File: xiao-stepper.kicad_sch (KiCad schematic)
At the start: 16 parts, among them J1 Conn_PinHeader_1x04_P2.54mm_H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, M1 XIAO-RP2040_SocketSMD

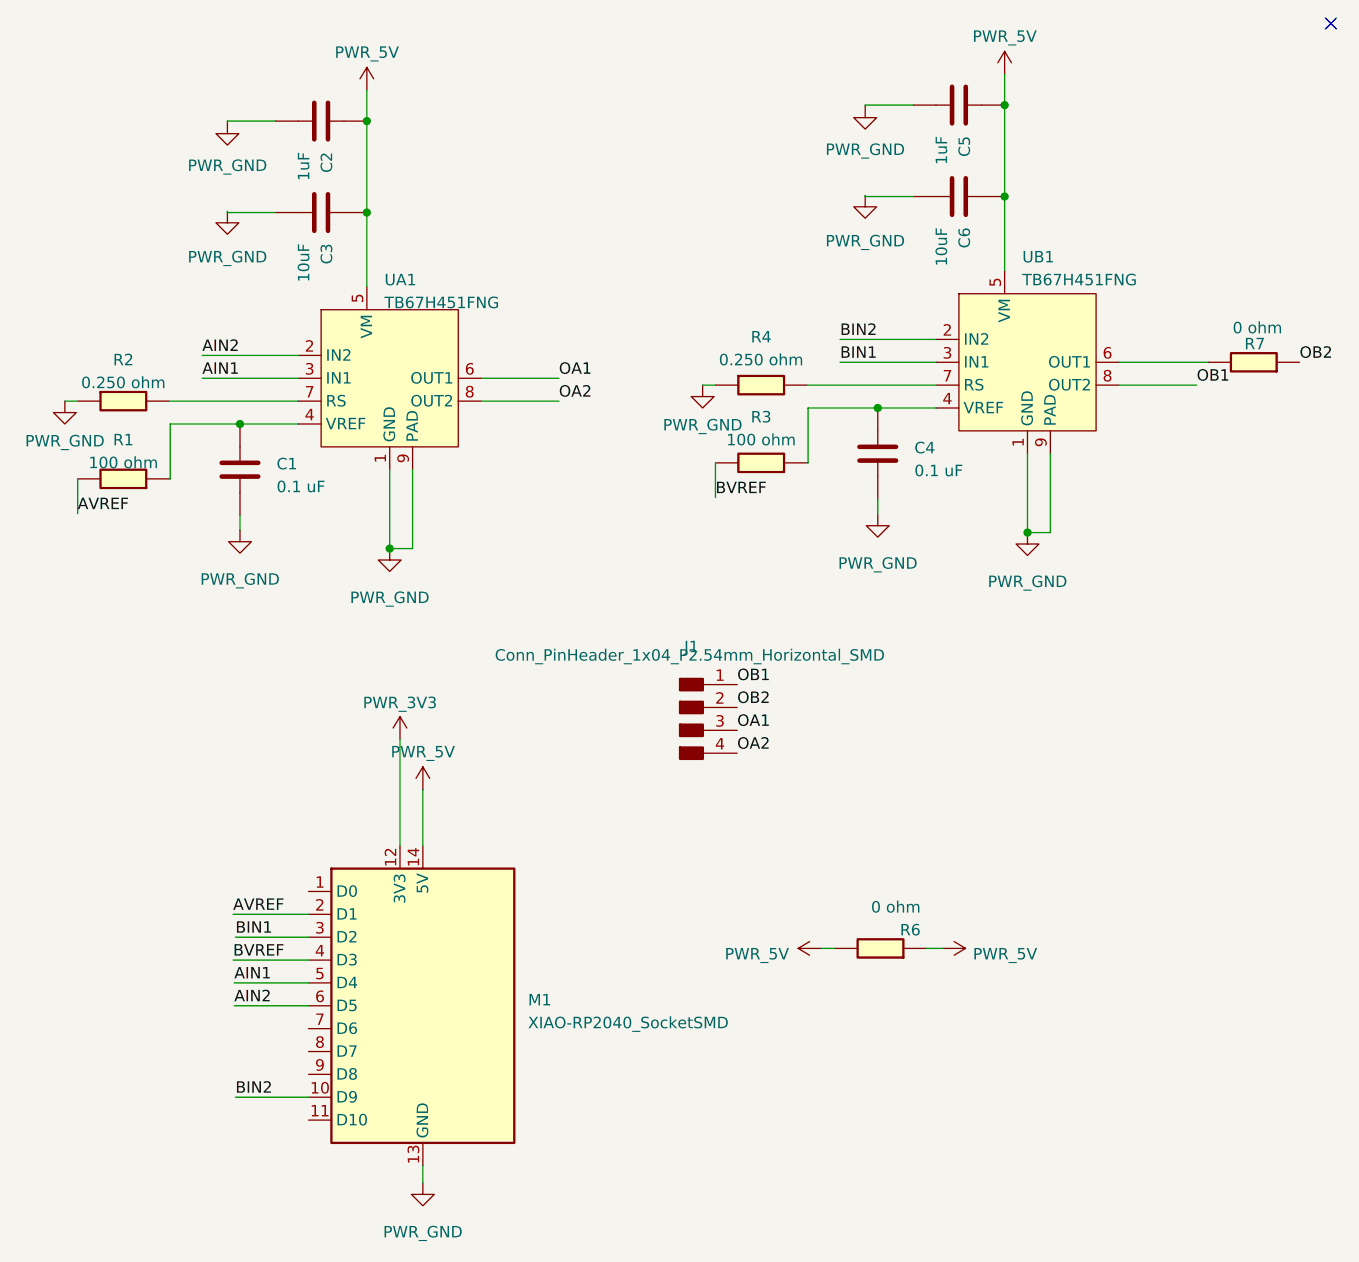
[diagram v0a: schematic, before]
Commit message: Added images
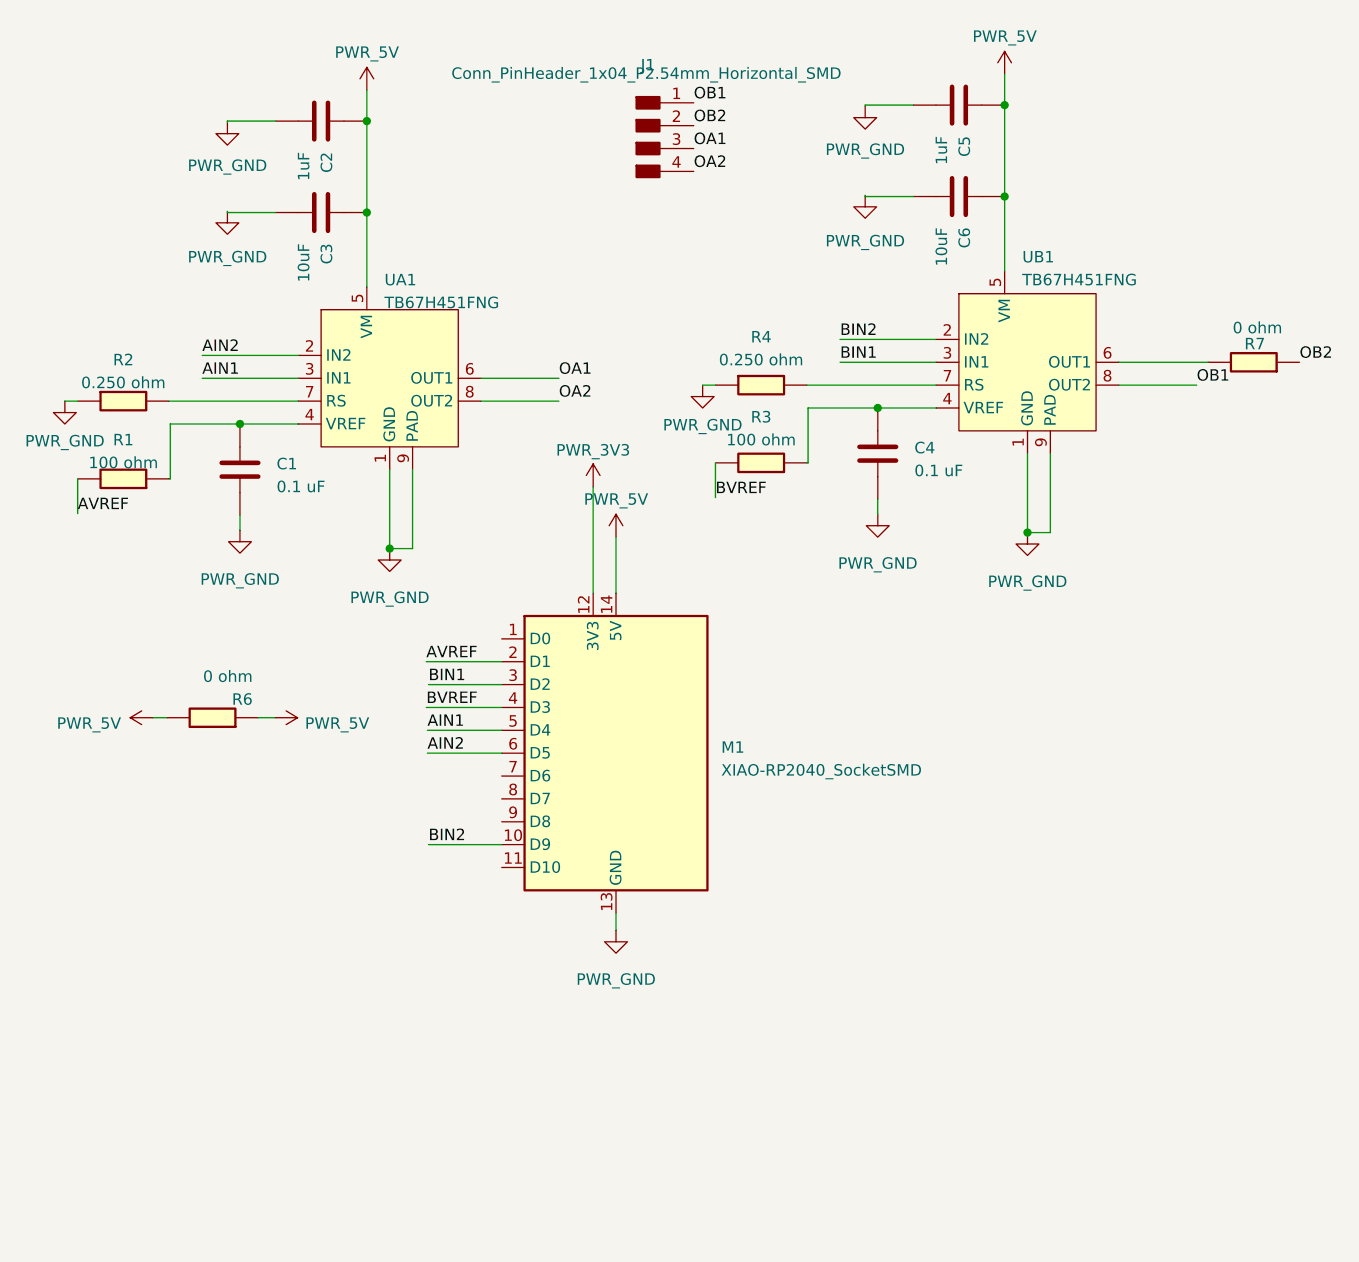
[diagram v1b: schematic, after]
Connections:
- no-connect marks 1 -> 0
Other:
- moved on the sheet: J1, M1, R6
